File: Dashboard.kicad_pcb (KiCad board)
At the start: 2 copper layers, 176.5 x 121.5 mm, 162 parts, among them J1 Left_Signal, J10 AccelConn, J11 BrakeConn, J12 AccelConn2, J13 BrakeConn2, J14 Motor-P, J15 Motor-C, J16 Array-C, J17 Array-P, J18 PowerConn, J19 CAN_OUT, J2 Right_Signal, J20 MotorCANConnector, J21 CAN_IN, J22 CAN_OUT, J23 USB_B_Micro, J24 ExtraGPIO_Conn, J25 UART_TP, J26 CAN_TP, J27 CAN_TP, J28 KILL_SW_IND, J3 Brake Light, J4 Headlight, J5 MinionConn, J6 SPI, J7 BPS_PWR_OUT, J8 JTAG, J9 POW_2ND_CONN, SW10 RESET, SW8 SW_Rotary2x6, U1 EL3H7, U10 EL3H7, U11 EL3H7, U12 RI3-1205S, U13 NCP1117-3.3_SOT223, U14 ADM3055E, U15 CDSOT23-T24CAN, U16 LTC6820, U17 ADM3055E, U18 CDSOT23-T24CAN, U19 CP2102N-A01-GQFN24, U2 EL3H7, U20 HX1188FNL, U3 EL3H7, U4 EL3H7, U5 EL3H7, U6 EL3H7, U7 STM32F413RHTx, U8 EL3H7, U9 EL3H7, Y1 Crystal

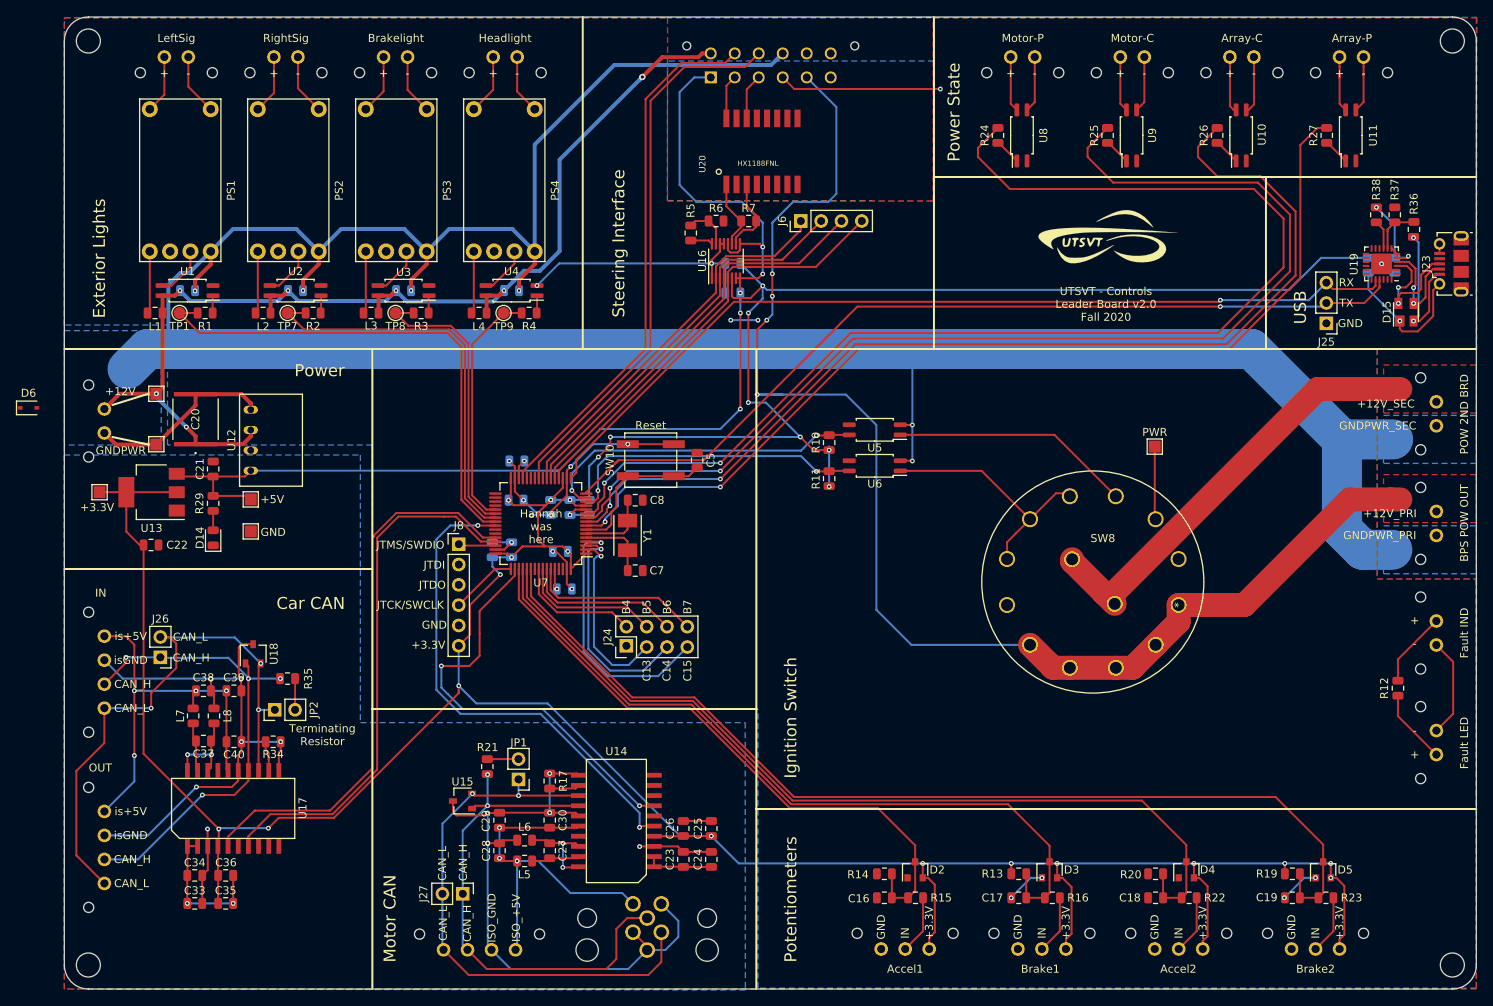
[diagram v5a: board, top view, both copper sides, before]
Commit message: Connects pots to ADC pins and removes JTAG connections
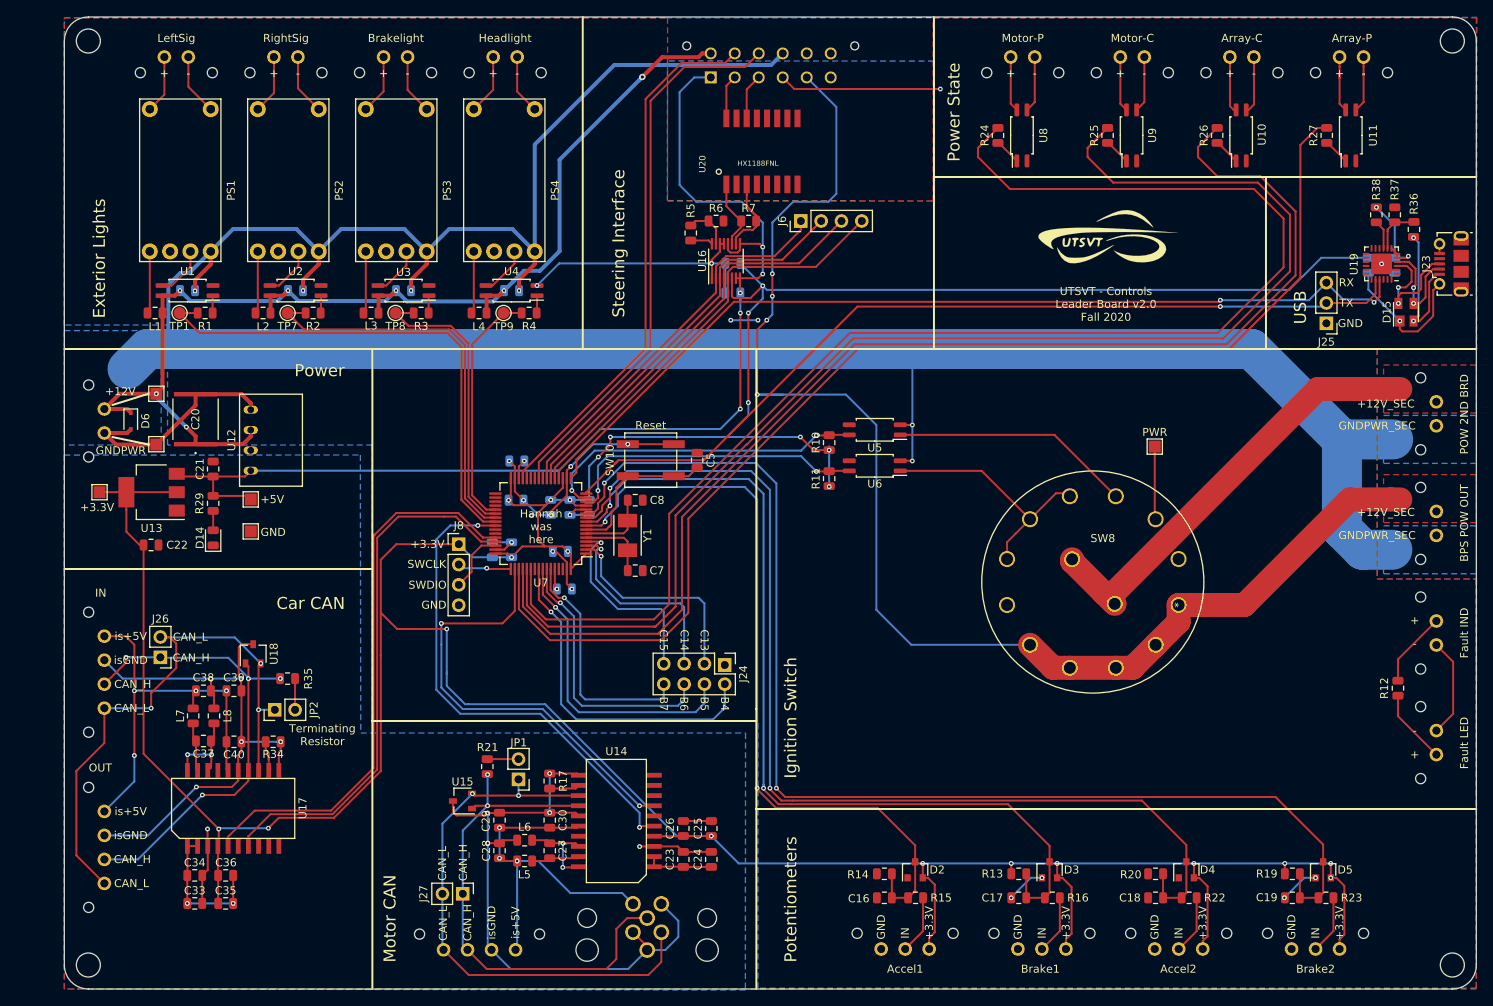
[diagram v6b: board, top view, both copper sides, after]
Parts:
- J8: value JTAG -> SWD; footprint Connector_PinHeader_2.54mm:PinHeader_1x06_P2.54mm_Vertical -> Connector_PinHeader_2.54mm:PinHeader_1x04_P2.54mm_Vertical
- moved D6 12.9 mm to (39.3, 104.0), turned to 270 degrees
- moved J24 12.5 mm to (113.5, 134.3), turned to 270 degrees
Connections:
- J8 pad 1: /SWDIO -> +3V3
- J8 pad 2: /JTDI -> /SWCLK
- J8 pad 3: /JTDO -> /SWDIO
- J8 pad 4: /SWCLK -> GND
- U7 pad 10: /M_CNCTR -> /Accel_Pot2
- U7 pad 11: /M_PRCHG -> /Brake_Pot2
- U7 pad 51: /Accel_Pot -> /A_PRCHG
- U7 pad 52: /Brake_Pot -> /A_CNCTR
- U7 pad 53: /Accel_Pot2 -> /M_CNCTR
- U7 pad 54: /Brake_Pot2 -> /M_PRCHG
- U7 pad 8: /A_PRCHG -> /Accel_Pot
- U7 pad 9: /A_CNCTR -> /Brake_Pot
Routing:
- net /PB4: track 15.8 -> 42.9 mm, vias 0 -> 1
- net /A_PRCHG: track 125.1 -> 152.0 mm, vias 2 -> 0
- net /A_CNCTR: track 130.1 -> 155.9 mm, vias 2 -> 0
- net /M_CNCTR: track 141.8 -> 166.2 mm, vias 2 -> 0
- net +3V3: track 511.9 -> 535.6 mm, vias 27 -> 26
- net /Brake_Pot2: track 127.5 -> 150.4 mm, vias 0 -> 2
- net /M_PRCHG: track 153.5 -> 176.3 mm, vias 2 -> 0
- net /Accel_Pot2: track 111.0 -> 131.9 mm, vias 0 -> 2
- net /PB5: track 17.7 -> 38.3 mm, vias 0 -> 1
- net /Brake_Pot: track 94.4 -> 113.7 mm, vias 0 -> 2
- net /Accel_Pot: track 78.0 -> 95.9 mm, vias 0 -> 2
- net /PB6: track 19.7 -> 34.2 mm, vias 0 -> 1
- net /PC15: track 33.3 -> 24.8 mm
- net /PB7: track 21.6 -> 30.1 mm, vias 0 -> 1
- net /PC13: track 22.6 -> 26.6 mm
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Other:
- board text added: "SWCLK"
- board text added: "SWDIO"
- board text removed: "+12V_PRI"
- board text removed: "GNDPWR_PRI"
- board text removed: "ISO_+5V"
- board text removed: "ISO_GND"
- board text removed: "JTCK/SWCLK"
- board text removed: "JTDI"
- board text removed: "JTDO"
- board text removed: "JTMS/SWDIO"

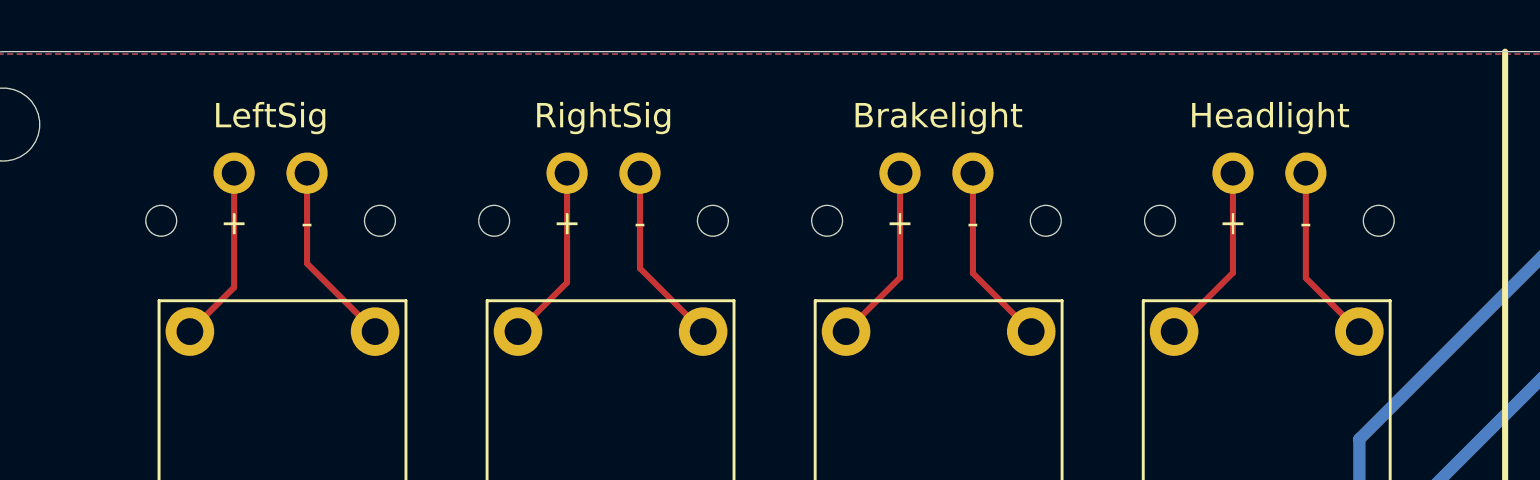
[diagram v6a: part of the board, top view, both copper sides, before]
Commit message: Flips exterior lights polarity on the connectors
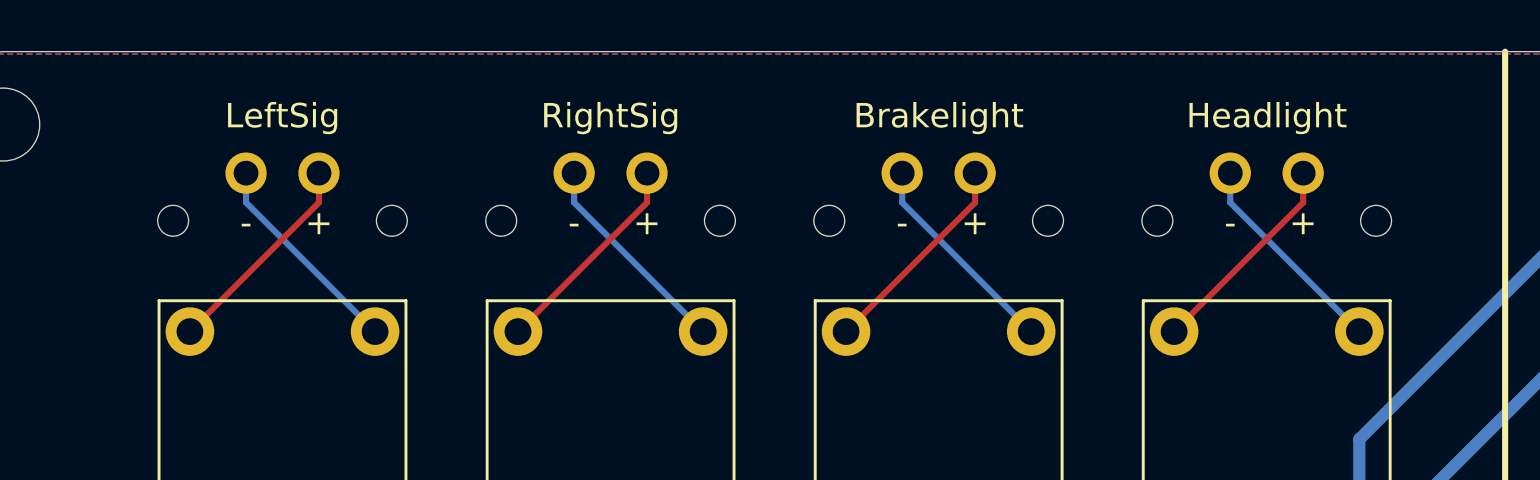
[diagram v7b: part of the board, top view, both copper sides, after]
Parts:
- moved J1 0.49 mm to (44.0, 58.5)
- moved J2 0.29 mm to (57.5, 58.5)
- moved J4 0.11 mm to (84.5, 58.5)
- moved J3 0.09 mm to (71.0, 58.5)
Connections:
- PS1 pad 5: Net-(J1-Pad2) -> Net-(J1-Pad1)
- PS1 pad 6: Net-(J1-Pad1) -> Net-(J1-Pad2)
- PS2 pad 5: Net-(J2-Pad2) -> Net-(J2-Pad1)
- PS2 pad 6: Net-(J2-Pad1) -> Net-(J2-Pad2)
- PS3 pad 5: Net-(J3-Pad2) -> Net-(J3-Pad1)
- PS3 pad 6: Net-(J3-Pad1) -> Net-(J3-Pad2)
- PS4 pad 5: Net-(J4-Pad2) -> Net-(J4-Pad1)
- PS4 pad 6: Net-(J4-Pad1) -> Net-(J4-Pad2)
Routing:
- net Net-(J1-Pad1): track 7.27 -> 8.72 mm
- net Net-(J2-Pad1): track 7.36 -> 8.72 mm
- net Net-(J4-Pad2): track 7.43 -> 8.72 mm
- net Net-(J3-Pad1): track 7.44 -> 8.72 mm
- net Net-(J3-Pad2): track 7.51 -> 8.72 mm
- net Net-(J4-Pad1): track 7.52 -> 8.72 mm
- net Net-(J2-Pad2): track 7.60 -> 8.72 mm
- net Net-(J1-Pad2): track 7.68 -> 8.72 mm

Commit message: Updates gerbers and version number
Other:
- board text added: "UTSVT - Controls Leader Board v2.1 Fall 2020"
- board text removed: "UTSVT - Controls Leader Board v2.0 Fall 2020"
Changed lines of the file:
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@@
     (effects (font (size 2 2) (thickness 0.3)) (justify mirror))
   )
-  (gr_text "UTSVT - Controls\nLeader Board v2.0\nFall 2020" (at 161.2 89.4) (layer F.SilkS)
+  (gr_text "UTSVT - Controls\nLeader Board v2.1\nFall 2020" (at 161.2 89.4) (layer F.SilkS)
     (effects (font (size 1 1) (thickness 0.15)))
   )
